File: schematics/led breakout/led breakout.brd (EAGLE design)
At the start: 16.8 x 8.9 mm, 3 parts

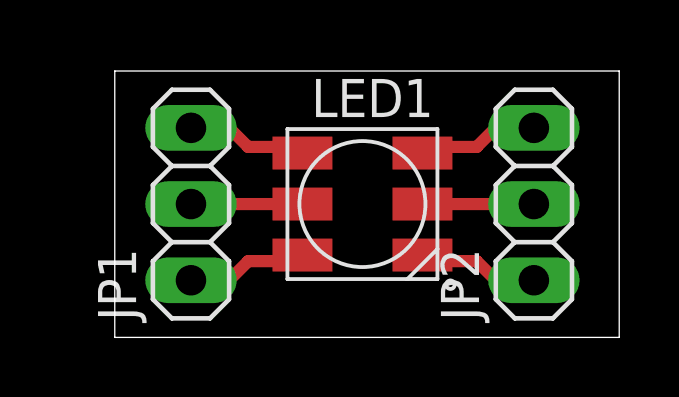
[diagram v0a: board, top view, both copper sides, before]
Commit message: Had wrong pin headers (too small), but worked out since the difference is not that big and there are only 3 pins on each side.
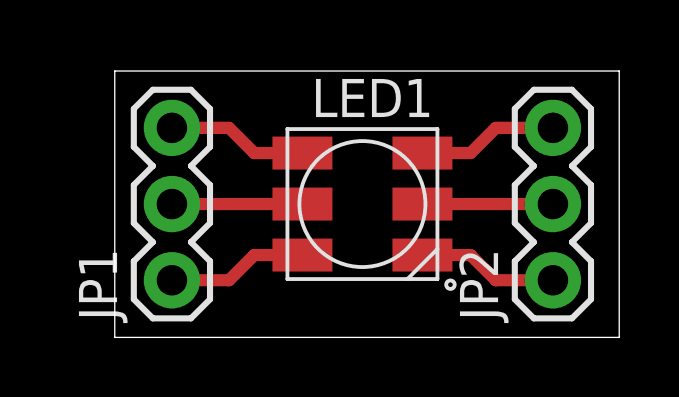
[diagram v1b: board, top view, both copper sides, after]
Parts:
- JP1, JP2: device pinhead:1X03 -> SparkFun-Connectors:1X03
- moved JP1 2.62 mm to (1.91, 1.91)
- moved JP2 2.62 mm to (14.6, 1.91)
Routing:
- net N$6: track 3.44 -> 4.70 mm
- net N$4: track 3.44 -> 4.70 mm
- net N$5: track 3.18 -> 4.35 mm
- net N$3: track 4.07 -> 4.70 mm
- net N$1: track 4.07 -> 4.70 mm
- net N$2: track 3.81 -> 4.35 mm
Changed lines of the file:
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@@
 <layer number="97" name="Info" color="7" fill="1" visible="no" active="no"/>
 <layer number="98" name="Guide" color="6" fill="1" visible="no" active="no"/>
+<layer number="99" name="SpiceOrder" color="7" fill="1" visible="no" active="no"/>
 <layer number="100" name="Muster" color="7" fill="1" visible="no" active="no"/>
 <layer number="101" name="Patch_Top" color="12" fill="4" visible="yes" active="yes"/>
@@
 <layer number="111" name="LPC17xx" color="7" fill="1" visible="yes" active="yes"/>
 <layer number="112" name="tSilk" color="7" fill="1" visible="yes" active="yes"/>
+<layer number="113" name="IDFDebug" color="4" fill="1" visible="yes" active="yes"/>
 <layer number="116" name="Patch_BOT" color="9" fill="4" visible="yes" active="yes"/>
 <layer number="121" name="_tsilk" color="7" fill="1" visible="yes" active="yes"/>
@@
 <elements>
 <element name="LED1" library="adafruit" package="RGBLED5050" value="RGBLED5050" x="8.255" y="4.445"/>
-<element name="JP1" library="pinhead" package="1X03" value="" x="2.54" y="4.445" rot="R90"/>
-<element name="JP2" library="pinhead" package="1X03" value="" x="13.97" y="4.445" rot="R90"/>
+<element name="JP1" library="SparkFun-Connectors" package="1X03" value="" x="1.905" y="1.905" rot="R90"/>
+<element name="JP2" library="SparkFun-Connectors" package="1X03" value="" x="14.605" y="1.905" rot="R90"/>
 </elements>
 <signals>
 <signal name="N$4">
+<contactref element="LED1" pad="4"/>
 <contactref element="JP2" pad="1"/>
-<contactref element="LED1" pad="4"/>
-<wire x1="13.97" y1="1.905" x2="12.7" y2="1.905" width="0.4064" layer="1"/>
-<wire x1="12.7" y1="1.905" x2="12.065" y2="2.54" width="0.4064" layer="1"/>
-<wire x1="12.065" y1="2.54" x2="10.795" y2="2.54" width="0.4064" layer="1"/>
-<wire x1="10.795" y1="2.54" x2="10.255" y2="2.745" width="0" layer="19" extent="1-1"/>
+<wire x1="10.255" y1="2.745" x2="11.86" y2="2.745" width="0.4064" layer="1"/>
+<wire x1="11.86" y1="2.745" x2="12.7" y2="1.905" width="0.4064" layer="1"/>
+<wire x1="12.7" y1="1.905" x2="14.605" y2="1.905" width="0.4064" layer="1"/>
 </signal>
 <signal name="N$1">
+<contactref element="LED1" pad="1"/>
 <contactref element="JP1" pad="3"/>
-<contactref element="LED1" pad="1"/>
-<wire x1="2.54" y1="6.985" x2="3.81" y2="6.985" width="0.4064" layer="1"/>
-<wire x1="3.81" y1="6.985" x2="4.445" y2="6.35" width="0.4064" layer="1"/>
-<wire x1="4.445" y1="6.35" x2="6.35" y2="6.35" width="0.4064" layer="1"/>
-<wire x1="6.35" y1="6.35" x2="6.255" y2="6.145" width="0" layer="19" extent="1-1"/>
+<wire x1="6.255" y1="6.145" x2="4.65" y2="6.145" width="0.4064" layer="1"/>
+<wire x1="4.65" y1="6.145" x2="3.81" y2="6.985" width="0.4064" layer="1"/>
+<wire x1="3.81" y1="6.985" x2="1.905" y2="6.985" width="0.4064" layer="1"/>
 </signal>
 <signal name="N$2">
+<contactref element="LED1" pad="2"/>
 <contactref element="JP1" pad="2"/>
-<contactref element="LED1" pad="2"/>
-<wire x1="2.54" y1="4.445" x2="6.35" y2="4.445" width="0.4064" layer="1"/>
-<wire x1="6.35" y1="4.445" x2="6.255" y2="4.445" width="0" layer="19" extent="1-1"/>
+<wire x1="6.255" y1="4.445" x2="1.905" y2="4.445" width="0.4064" layer="1"/>
 </signal>
 <signal name="N$3">
+<contactref element="LED1" pad="3"/>
 <contactref element="JP1" pad="1"/>
-<contactref element="LED1" pad="3"/>
-<wire x1="2.54" y1="1.905" x2="3.81" y2="1.905" width="0.4064" layer="1"/>
-<wire x1="3.81" y1="1.905" x2="4.445" y2="2.54" width="0.4064" layer="1"/>
-<wire x1="4.445" y1="2.54" x2="6.35" y2="2.54" width="0.4064" layer="1"/>
-<wire x1="6.35" y1="2.54" x2="6.255" y2="2.745" width="0" layer="19" extent="1-1"/>
+<wire x1="6.255" y1="2.745" x2="4.65" y2="2.745" width="0.4064" layer="1"/>
+<wire x1="4.65" y1="2.745" x2="3.81" y2="1.905" width="0.4064" layer="1"/>
+<wire x1="3.81" y1="1.905" x2="1.905" y2="1.905" width="0.4064" layer="1"/>
 </signal>
 <signal name="N$5">
 <contactref element="LED1" pad="5"/>
 <contactref element="JP2" pad="2"/>
-<wire x1="13.97" y1="4.445" x2="10.795" y2="4.445" width="0.4064" layer="1"/>
-<wire x1="10.795" y1="4.445" x2="10.255" y2="4.445" width="0" layer="19" extent="1-1"/>
+<wire x1="10.255" y1="4.445" x2="14.605" y2="4.445" width="0.4064" layer="1"/>
 </signal>
 <signal name="N$6">
 <contactref element="LED1" pad="6"/>
 <contactref element="JP2" pad="3"/>
-<wire x1="13.97" y1="6.985" x2="12.7" y2="6.985" width="0.4064" layer="1"/>
-<wire x1="12.7" y1="6.985" x2="12.065" y2="6.35" width="0.4064" layer="1"/>
-<wire x1="12.065" y1="6.35" x2="10.795" y2="6.35" width="0.4064" layer="1"/>
-<wire x1="10.795" y1="6.35" x2="10.255" y2="6.145" width="0" layer="19" extent="1-1"/>
+<wire x1="10.255" y1="6.145" x2="11.86" y2="6.145" width="0.4064" layer="1"/>
+<wire x1="11.86" y1="6.145" x2="12.7" y2="6.985" width="0.4064" layer="1"/>
+<wire x1="12.7" y1="6.985" x2="14.605" y2="6.985" width="0.4064" layer="1"/>
 </signal>
 </signals>
